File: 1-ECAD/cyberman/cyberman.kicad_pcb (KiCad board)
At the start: 6 copper layers, 0 parts

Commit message: footpritn day
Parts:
- added J1: 5033981892, 0_connector_smd:5033981892, F.Cu at (133.8, 86.6)
- added J2: YXT-BB10-24S-02, 0_connector_smd:YXT-BB10-24S-02, F.Cu at (162.8, 99.5)
- added J3: 532610271, 0_connector_smd:532610271, F.Cu at (128.7, 115.9)
- added L6: BLM15PX331SZ1D, 0_inductor_smd:BLM15PX331SZ1D, F.Cu at (128.3, 111.2)
- added L7: BLM15PX331SZ1D, 0_inductor_smd:BLM15PX331SZ1D, F.Cu at (129.3, 111.2)
- added U1: ESP32-S3R16V, 0_mcu_espressif:ESP32-S3R16V, F.Cu at (160.6, 87.7)
- added U11: LSM6DSOTR, 0_sensor:LSM6DSOTR, F.Cu at (139.1, 99.2)
- added U12: ICS-43434, 0_sensor:ICS-43434, F.Cu at (134.8, 107.3)
- added U13: MAX98357A, 0_CI_smd:MAX98357AETE+T, F.Cu at (129.3, 107.9)
- added U15: W25Q128JWPIQ, 0_CI_smd:W25Q128JWPIQ, F.Cu at (160.2, 77.2)
- added U16: 1054500101, 0_connector_smd:1054500101, F.Cu at (161.6, 68.5)
- added U18: PM254-2-10-W-8.5, 0_connector_smd:PM254-2-10-W-8.5, F.Cu at (151.2, 74.1)
- added U2: BQ25896RTWR, 0_CI_smd:BQ25896RTWR, F.Cu at (147.3, 100.4)
- added U20: LIS2MDLTR, 0_sensor:LIS2MDLTR, F.Cu at (139.7, 107.0)
- added U4: BQ27220YZFR, 0_CI_smd:BQ27220YZFR, F.Cu at (145.6, 109.2)
- added U5: RS3221-3.3YF3, 0_converter_DCDC:RS3221-3.3YF3, F.Cu at (153.2, 106.4)
- added U6: LM3281YFQR, 0_converter_DCDC:LM3281YFQR, F.Cu at (145.4, 105.6)
- added U7: LM3281YFQR, 0_converter_DCDC:LM3281YFQR, F.Cu at (148.7, 105.6)
- added U8: MMDT2907A-7-F, 0_CI_smd:MMDT2907A-7-F, F.Cu at (153.1, 98.9)

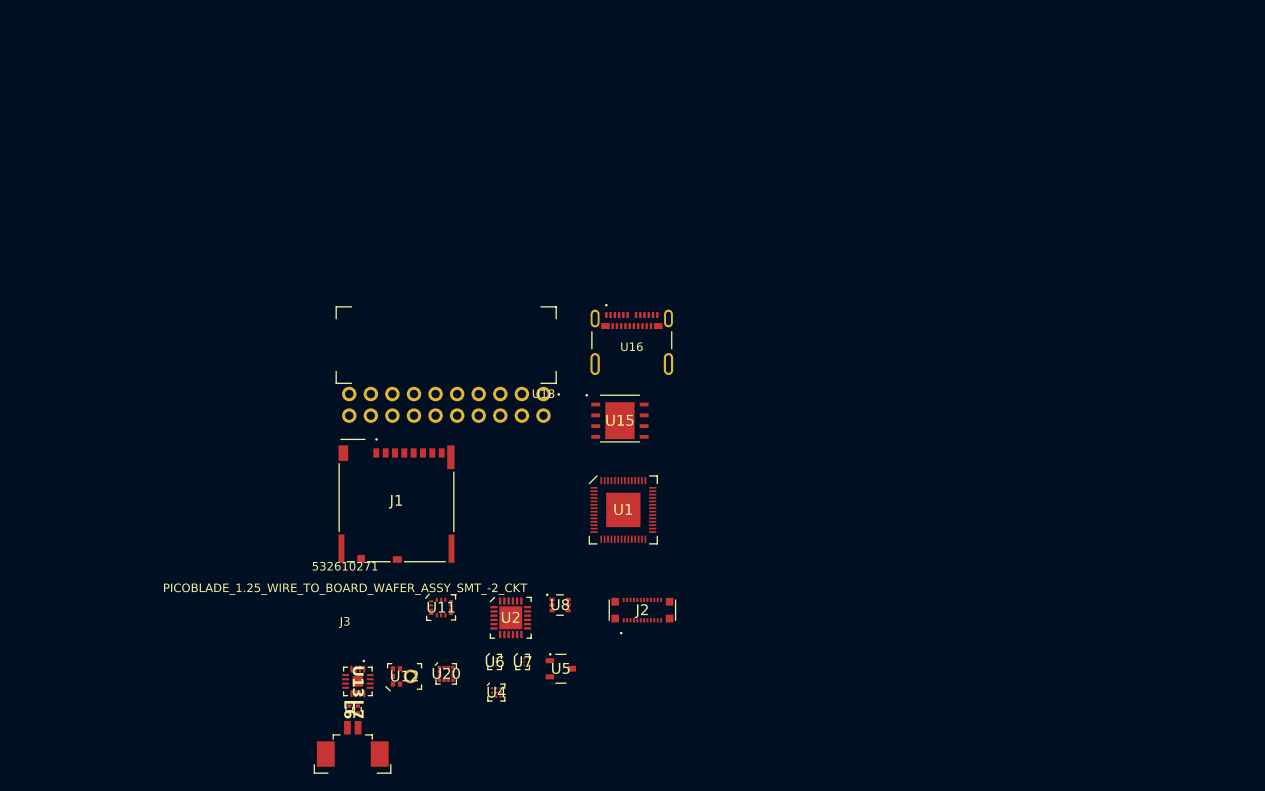
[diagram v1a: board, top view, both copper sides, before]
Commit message: sensor page closed
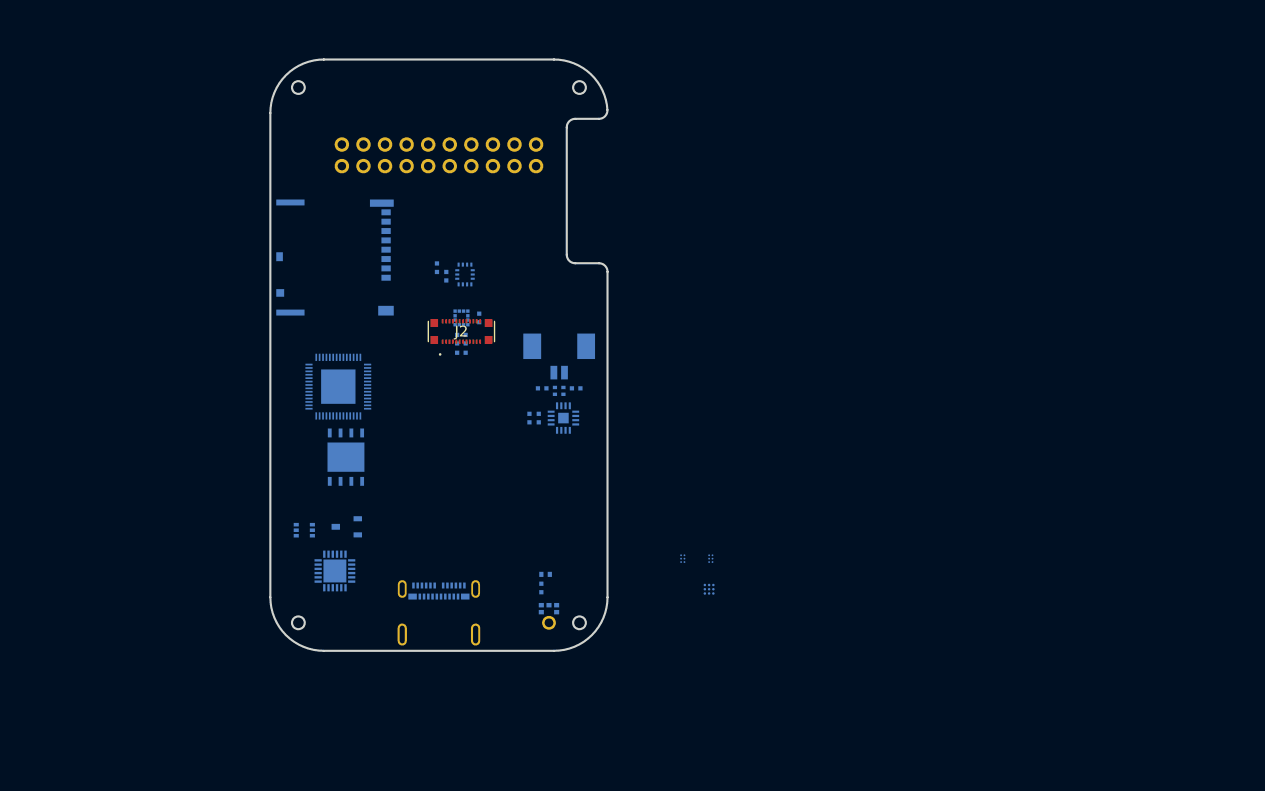
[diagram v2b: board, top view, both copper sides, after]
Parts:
- added C34: CC0402KRX7R8BB104, 0_capacitor_smd:C_0402, B.Cu at (138.6, 59.2)
- added C35: CC0402KRX7R8BB104, 0_capacitor_smd:C_0402, B.Cu at (139.7, 60.2)
- added C36: CC0402KRX7R8BB104, 0_capacitor_smd:C_0402, B.Cu at (141.5, 67.1)
- added C37: CC0402KRX7R8BB104, 0_capacitor_smd:C_0402, B.Cu at (141.5, 68.1)
- added C38: CC0402MRX5R6BB106, 0_capacitor_smd:C_0402, B.Cu at (141.5, 69.2)
- added C39: CC0402KRX7R8BB104, 0_capacitor_smd:C_0402, B.Cu at (150.9, 96.9)
- added C40: CC0402KRX7R8BB104, 0_capacitor_smd:C_0402, B.Cu at (150.6, 76.9)
- added C41: CC0402MRX5R6BB106, 0_capacitor_smd:C_0402, B.Cu at (149.5, 76.9)
- added C49: CC0402KRX5R8BB224, 0_capacitor_smd:C_0402, B.Cu at (143.6, 65.1)
- added C52: CC0402KRX7R8BB221, 0_capacitor_smd:C_0402, B.Cu at (155.0, 73.4)
- added C53: CC0402KRX7R8BB221, 0_capacitor_smd:C_0402, B.Cu at (151.0, 73.4)
- added R27: RC0402FR-07100KL, 0_resistor_smd:R_0402, B.Cu at (151.4, 95.3)
- J1, J3, L6, L7, U1, U11, U12, U13, U15, U16, U18, U2, U20, U4, U5, U6, U7, U8: moved to B.Cu
- moved J3 52.8 mm to (153.0, 69.0)
- moved L6 44.6 mm to (152.5, 73.7), turned to 90 degrees
- moved L7 44.6 mm to (153.5, 73.7), turned to 90 degrees
- moved U20 41.9 mm to (141.5, 65.1), turned to -90 degrees
- moved U13 39.3 mm to (153.5, 76.9), turned to 90 degrees
- moved U11 39.3 mm to (141.9, 60.0), turned to 90 degrees
- moved J2 39.1 mm to (141.5, 66.7)
- moved U16 39.1 mm to (138.8, 100.4), turned to 180 degrees
- moved U18 37.8 mm to (127.4, 44.7), turned to 180 degrees
- moved U1 36.6 mm to (127.0, 73.2), turned to -90 degrees
- moved U15 32.5 mm to (127.9, 81.5), turned to 90 degrees
- moved U8 31.4 mm to (123.0, 90.1), turned to 180 degrees
- moved U5 30.2 mm to (128.0, 89.7), turned to 180 degrees
- moved J1 29.4 mm to (127.0, 58.0), turned to 90 degrees
- moved U6 28.2 mm to (170.8, 93.5), turned to 180 degrees
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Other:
- board outline added: 39.7 x 69.6 mm
- copper layers 6 -> 4

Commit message: add buttons
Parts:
- added SW1: SKRMAAE010, 0_switch:SKRMAAE010, F.Cu at (149.1, 83.8)
- added SW2: SKRMAAE010, 0_switch:SKRMAAE010, F.Cu at (149.1, 94.2)
- added SW3: SKRMAAE010, 0_switch:SKRMAAE010, F.Cu at (130.5, 81.5)
- added SW4: SKRMAAE010, 0_switch:SKRMAAE010, F.Cu at (138.0, 89.0)
- added SW5: SKRMAAE010, 0_switch:SKRMAAE010, F.Cu at (123.0, 89.0)
- added SW6: SKRMAAE010, 0_switch:SKRMAAE010, F.Cu at (130.5, 96.5)
- moved C39 25.8 mm to (125.1, 96.9)
- moved C52 25.8 mm to (129.2, 73.4)
- moved R27 25.8 mm to (125.6, 95.3)
- moved U12 25.8 mm to (126.0, 100.3)
- moved C40 25.8 mm to (124.8, 76.9)
- moved C41 25.8 mm to (123.7, 76.9)
- moved C53 25.8 mm to (125.2, 73.4)
- moved J3 25.8 mm to (127.2, 69.0)
- moved L6 25.8 mm to (126.7, 73.7)
- moved L7 25.8 mm to (127.7, 73.7)
- moved U13 25.8 mm to (127.7, 76.9)
- moved J1 24.8 mm to (151.7, 59.6)
- moved U1 24.5 mm to (151.4, 74.8)
- moved U15 24.5 mm to (152.3, 83.1)
- moved U2 24.5 mm to (151.0, 96.5)
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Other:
- outline, holes or cut-outs redrawn

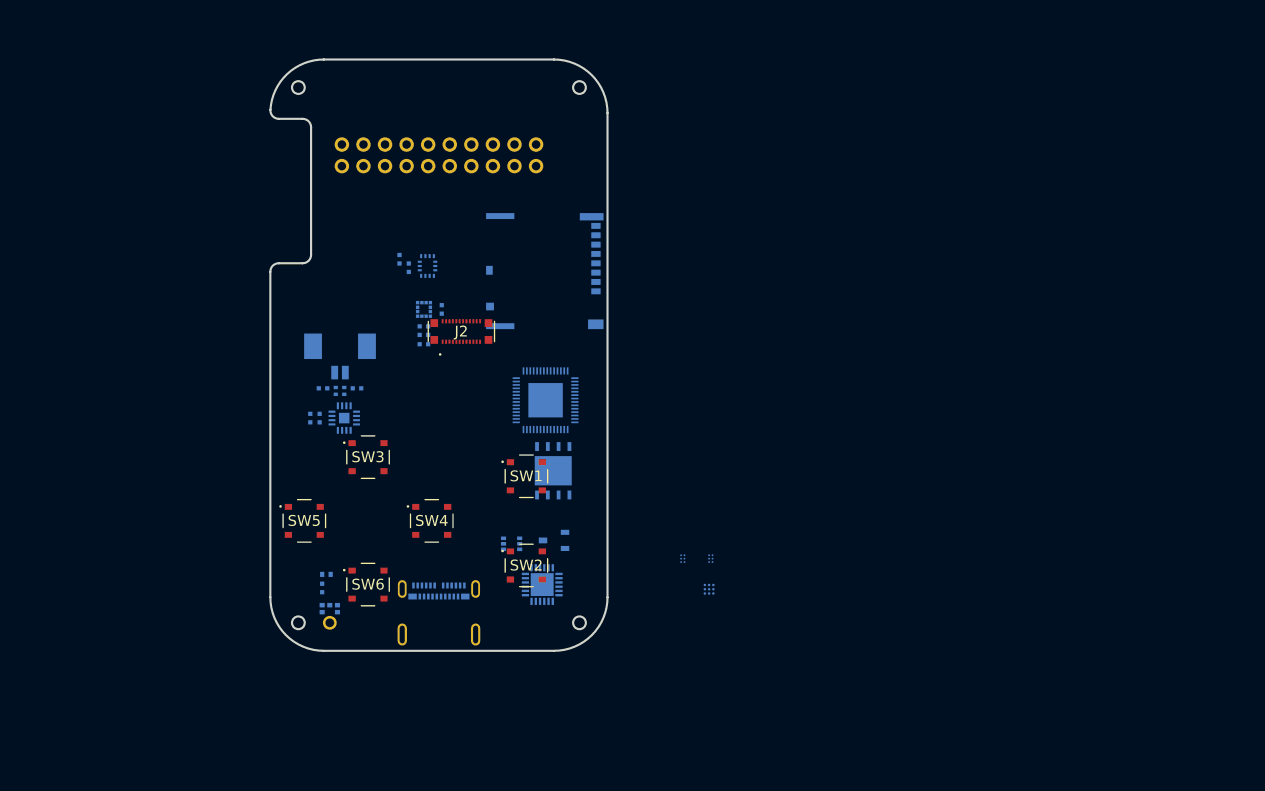
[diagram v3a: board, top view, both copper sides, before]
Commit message: new changes
close display page and peripheral schematic
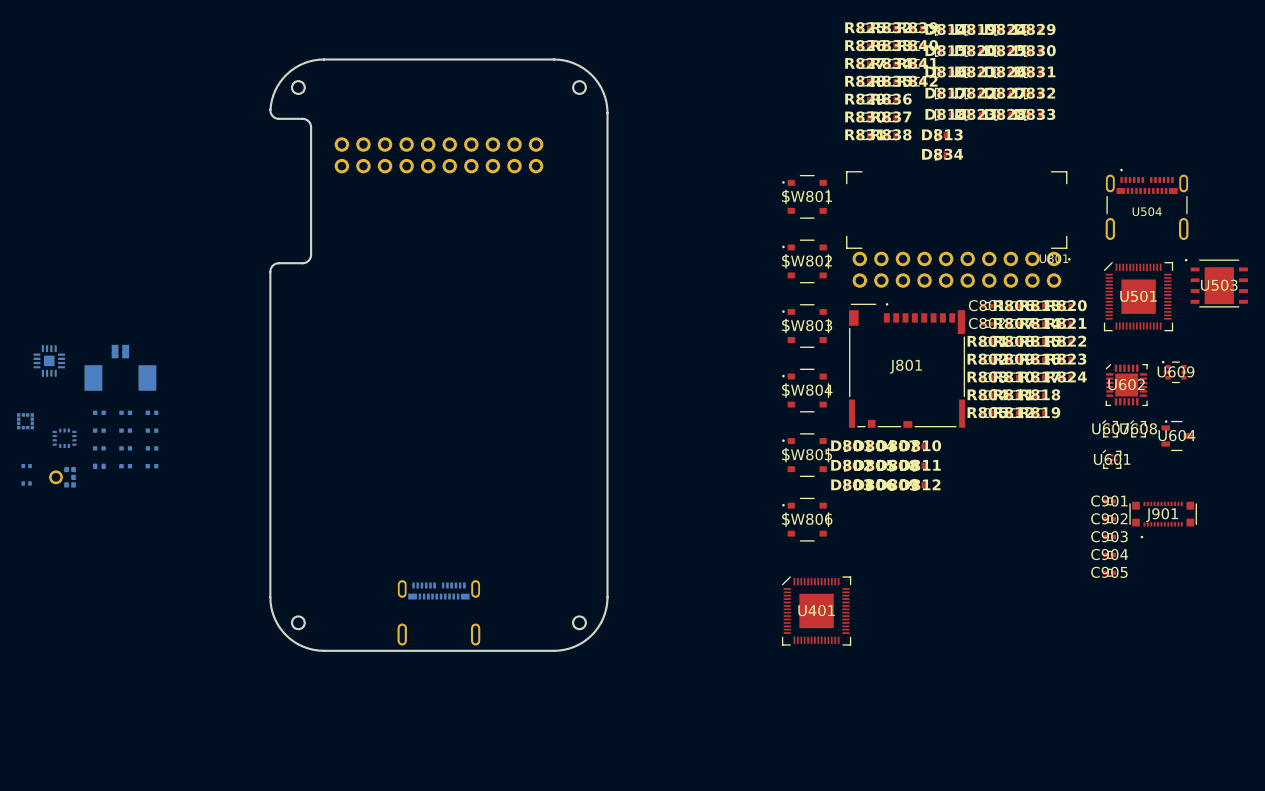
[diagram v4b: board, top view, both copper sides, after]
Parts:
- removed C34, C35, C36, C37, C39, C40: CC0402KRX7R8BB104, 0_capacitor_smd:C_0402
- removed C38, C41: CC0402MRX5R6BB106, 0_capacitor_smd:C_0402
- removed C49: CC0402KRX5R8BB224, 0_capacitor_smd:C_0402
- removed C52, C53: CC0402KRX7R8BB221, 0_capacitor_smd:C_0402
- removed J1: 5033981892, 0_connector_smd:5033981892
- removed J2: YXT-BB10-24S-02, 0_connector_smd:YXT-BB10-24S-02
- removed J3: 532610271, 0_connector_smd:532610271
- removed L6, L7: BLM15PX331SZ1D, 0_inductor_smd:BLM15PX331SZ1D
- removed R27: RC0402FR-07100KL, 0_resistor_smd:R_0402
- removed SW1, SW2, SW3, SW4, SW5, SW6: SKRMAAE010, 0_switch:SKRMAAE010
- removed U1: ESP32-S3R16V, 0_mcu_espressif:ESP32-S3R16V
- removed U11: LSM6DSOTR, 0_sensor:LSM6DSOTR
- removed U12: ICS-43434, 0_sensor:ICS-43434
- removed U13: MAX98357A, 0_CI_smd:MAX98357AETE+T
- removed U15: W25Q128JWPIQ, 0_CI_smd:W25Q128JWPIQ
- removed U2: BQ25896RTWR, 0_CI_smd:BQ25896RTWR
- removed U20: LIS2MDLTR, 0_sensor:LIS2MDLTR
- removed U4: BQ27220YZFR, 0_CI_smd:BQ27220YZFR
- removed U5: RS3221-3.3YF3, 0_converter_DCDC:RS3221-3.3YF3
- removed U6, U7: LM3281YFQR, 0_converter_DCDC:LM3281YFQR
- removed U8: MMDT2907A-7-F, 0_CI_smd:MMDT2907A-7-F
- added C1001: CC0402MRX5R6BB106, 0_capacitor_smd:C_0402, B.Cu at (105.1, 76.3)
- added C1002: CC0402KRX7R8BB104, 0_capacitor_smd:C_0402, B.Cu at (105.1, 78.4)
- added C1003: CC0402KRX7R8BB104, 0_capacitor_smd:C_0402, B.Cu at (105.1, 80.5)
- added C1004: CC0402KRX7R8BB221, 0_capacitor_smd:C_0402, B.Cu at (105.1, 82.6)
- added C1005: CC0402KRX7R8BB221, 0_capacitor_smd:C_0402, B.Cu at (102.0, 76.3)
- added C1006: CC0402MRX5R6BB106, 0_capacitor_smd:C_0402, B.Cu at (102.0, 78.4)
- added C1007: CC0402KRX7R8BB104, 0_capacitor_smd:C_0402, B.Cu at (102.0, 80.5)
- added C1008: CC0402KRX7R8BB104, 0_capacitor_smd:C_0402, B.Cu at (102.0, 82.6)
- added C1009: CC0402KRX7R8BB104, 0_capacitor_smd:C_0402, B.Cu at (98.9, 76.3)
- added C1010: CC0402KRX7R8BB104, 0_capacitor_smd:C_0402, B.Cu at (98.9, 78.4)
- added C1011: CC0402KRX5R8BB224, 0_capacitor_smd:C_0402, B.Cu at (98.9, 80.5)
- added C801: CC0402MRX5R6BB106, 0_capacitor_smd:C_0402, F.Cu at (203.4, 63.7)
- added C802: CC0402MRX5R6BB106, 0_capacitor_smd:C_0402, F.Cu at (203.4, 65.8)
- added C901: CC0402MRX5R6BB106, 0_capacitor_smd:C_0402, F.Cu at (217.8, 86.7)
- added C902: CC0402KRX7R8BB104, 0_capacitor_smd:C_0402, F.Cu at (217.8, 88.8)
- added C903: CC0402KRX7R8BB104, 0_capacitor_smd:C_0402, F.Cu at (217.8, 90.9)
- added C904: CC0402MRX5R6BB106, 0_capacitor_smd:C_0402, F.Cu at (217.8, 93.0)
- added C905: CC0402KRX7R8BB104, 0_capacitor_smd:C_0402, F.Cu at (217.8, 95.1)
- added D801: LESD8D3.3CAT5G, 0_diode_smd:LESD8D3.3CAT5G, F.Cu at (187.4, 80.2)
- added D802: LESD8D3.3CAT5G, 0_diode_smd:LESD8D3.3CAT5G, F.Cu at (187.4, 82.5)
- added D803: LESD8D3.3CAT5G, 0_diode_smd:LESD8D3.3CAT5G, F.Cu at (187.4, 84.8)
- added D804: LESD8D3.3CAT5G, 0_diode_smd:LESD8D3.3CAT5G, F.Cu at (190.1, 80.2)
- added D805: LESD8D3.3CAT5G, 0_diode_smd:LESD8D3.3CAT5G, F.Cu at (190.1, 82.5)
- added D806: LESD8D3.3CAT5G, 0_diode_smd:LESD8D3.3CAT5G, F.Cu at (190.1, 84.8)
- added D807: LESD8D3.3CAT5G, 0_diode_smd:LESD8D3.3CAT5G, F.Cu at (192.8, 80.2)
- added D808: LESD8D3.3CAT5G, 0_diode_smd:LESD8D3.3CAT5G, F.Cu at (192.8, 82.5)
- added D809: LESD8D3.3CAT5G, 0_diode_smd:LESD8D3.3CAT5G, F.Cu at (192.8, 84.8)
- added D810: LESD8D3.3CAT5G, 0_diode_smd:LESD8D3.3CAT5G, F.Cu at (195.5, 80.2)
- added D811: LESD8D3.3CAT5G, 0_diode_smd:LESD8D3.3CAT5G, F.Cu at (195.5, 82.5)
- added D812: LESD8D3.3CAT5G, 0_diode_smd:LESD8D3.3CAT5G, F.Cu at (195.5, 84.8)
- added D813: LESD8D3.3CAT5G, 0_diode_smd:LESD8D3.3CAT5G, F.Cu at (198.1, 43.6)
- added D814: LESD5D5.0CT1G, 0_diode_smd:LESD5D5.0CT1G, F.Cu at (198.5, 31.2)
- added D815: LESD5D5.0CT1G, 0_diode_smd:LESD5D5.0CT1G, F.Cu at (198.5, 33.7)
- added D816: LESD5D5.0CT1G, 0_diode_smd:LESD5D5.0CT1G, F.Cu at (198.5, 36.2)
- added D817: LESD5D5.0CT1G, 0_diode_smd:LESD5D5.0CT1G, F.Cu at (198.5, 38.7)
- added D818: LESD5D5.0CT1G, 0_diode_smd:LESD5D5.0CT1G, F.Cu at (198.5, 41.2)
- added D819: LESD5D5.0CT1G, 0_diode_smd:LESD5D5.0CT1G, F.Cu at (202.0, 31.2)
- added D820: LESD5D5.0CT1G, 0_diode_smd:LESD5D5.0CT1G, F.Cu at (202.0, 33.7)
- added D821: LESD5D5.0CT1G, 0_diode_smd:LESD5D5.0CT1G, F.Cu at (202.0, 36.2)
- added D822: LESD5D5.0CT1G, 0_diode_smd:LESD5D5.0CT1G, F.Cu at (202.0, 38.7)
- added D823: LESD5D5.0CT1G, 0_diode_smd:LESD5D5.0CT1G, F.Cu at (202.0, 41.2)
- added D824: LESD5D5.0CT1G, 0_diode_smd:LESD5D5.0CT1G, F.Cu at (205.5, 31.2)
- added D825: LESD5D5.0CT1G, 0_diode_smd:LESD5D5.0CT1G, F.Cu at (205.5, 33.7)
- added D826: LESD5D5.0CT1G, 0_diode_smd:LESD5D5.0CT1G, F.Cu at (205.5, 36.2)
- added D827: LESD5D5.0CT1G, 0_diode_smd:LESD5D5.0CT1G, F.Cu at (205.5, 38.7)
- added D828: LESD5D5.0CT1G, 0_diode_smd:LESD5D5.0CT1G, F.Cu at (205.5, 41.2)
- added D829: LESD5D5.0CT1G, 0_diode_smd:LESD5D5.0CT1G, F.Cu at (209.0, 31.2)
- added D830: LESD5D5.0CT1G, 0_diode_smd:LESD5D5.0CT1G, F.Cu at (209.0, 33.7)
- added D831: LESD5D5.0CT1G, 0_diode_smd:LESD5D5.0CT1G, F.Cu at (209.0, 36.2)
- added D832: LESD5D5.0CT1G, 0_diode_smd:LESD5D5.0CT1G, F.Cu at (209.0, 38.7)
- added D833: LESD5D5.0CT1G, 0_diode_smd:LESD5D5.0CT1G, F.Cu at (209.0, 41.2)
- added D834: LESD8D3.3CAT5G, 0_diode_smd:LESD8D3.3CAT5G, F.Cu at (198.1, 45.9)
- added J1001: 532610271, 0_connector_smd:532610271, B.Cu at (101.3, 71.6)
- added J801: 5033981892, 0_connector_smd:5033981892, F.Cu at (193.9, 70.7)
- added J901: YXT-BB10-24S-02, 0_connector_smd:YXT-BB10-24S-02, F.Cu at (224.1, 88.2)
- added L1001: BLM15PX331SZ1D, 0_inductor_smd:BLM15PX331SZ1D, B.Cu at (90.3, 82.5)
- added L1002: BLM15PX331SZ1D, 0_inductor_smd:BLM15PX331SZ1D, B.Cu at (90.3, 84.6)
- added R1001: RC0402FR-07100KL, 0_resistor_smd:R_0402, B.Cu at (98.9, 82.6)
- added R801: RC0402FR-0747KL, 0_resistor_smd:R_0402, F.Cu at (203.4, 67.9)
- added R802: RC0402FR-0747KL, 0_resistor_smd:R_0402, F.Cu at (203.4, 70.0)
- added R803: RC0402FR-0747KL, 0_resistor_smd:R_0402, F.Cu at (203.4, 72.1)
- added R804: RC0402FR-0747KL, 0_resistor_smd:R_0402, F.Cu at (203.4, 74.2)
- added R805: RC0402FR-0747KL, 0_resistor_smd:R_0402, F.Cu at (203.4, 76.3)
- added R806: RC0402FR-0747KL, 0_resistor_smd:R_0402, F.Cu at (206.5, 63.7)
- added R807: RC0402FR-0747KL, 0_resistor_smd:R_0402, F.Cu at (206.5, 65.8)
- added R808: RC0402FR-0710KL, 0_resistor_smd:R_0402, F.Cu at (206.5, 67.9)
- added R809: RC0402FR-0710KL, 0_resistor_smd:R_0402, F.Cu at (206.5, 70.0)
- added R810: RC0402FR-0710KL, 0_resistor_smd:R_0402, F.Cu at (206.5, 72.1)
- added R811: RC0402FR-0710KL, 0_resistor_smd:R_0402, F.Cu at (206.5, 74.2)
- added R812: RC0402FR-0710KL, 0_resistor_smd:R_0402, F.Cu at (206.5, 76.3)
- added R813: RC0402FR-0710KL, 0_resistor_smd:R_0402, F.Cu at (209.6, 63.7)
- added R814: RC0402FR-07330RL, 0_resistor_smd:R_0402, F.Cu at (209.6, 65.8)
- added R815: RC0402FR-07150RL, 0_resistor_smd:R_0402, F.Cu at (209.6, 67.9)
- added R816: RC0402FR-0751RL, 0_resistor_smd:R_0402, F.Cu at (209.6, 70.0)
- added R817: RC0402FR-0751RL, 0_resistor_smd:R_0402, F.Cu at (209.6, 72.1)
- added R818: RC0402FR-07330RL, 0_resistor_smd:R_0402, F.Cu at (209.6, 74.2)
- added R819: RC0402FR-0751RL, 0_resistor_smd:R_0402, F.Cu at (209.6, 76.3)
- added R820: RC0402FR-07150RL, 0_resistor_smd:R_0402, F.Cu at (212.7, 63.7)
- added R821: RC0402FR-07330RL, 0_resistor_smd:R_0402, F.Cu at (212.7, 65.8)
- added R822: RC0402FR-07330RL, 0_resistor_smd:R_0402, F.Cu at (212.7, 67.9)
- added R823: RC0402FR-07330RL, 0_resistor_smd:R_0402, F.Cu at (212.7, 70.0)
- added R824: RC0402FR-07330RL, 0_resistor_smd:R_0402, F.Cu at (212.7, 72.1)
- added R825: RC0402FR-0751RL, 0_resistor_smd:R_0402, F.Cu at (189.0, 31.0)
- added R826: RC0402FR-0751RL, 0_resistor_smd:R_0402, F.Cu at (189.0, 33.1)
- added R827: RC0402FR-0751RL, 0_resistor_smd:R_0402, F.Cu at (189.0, 35.2)
- added R828: RC0402FR-0751RL, 0_resistor_smd:R_0402, F.Cu at (189.0, 37.3)
- added R829: RC0402FR-0751RL, 0_resistor_smd:R_0402, F.Cu at (189.0, 39.4)
- added R830: RC0402FR-0751RL, 0_resistor_smd:R_0402, F.Cu at (189.0, 41.5)
- added R831: RC0402FR-0751RL, 0_resistor_smd:R_0402, F.Cu at (189.0, 43.6)
- added R832: RC0402FR-0751RL, 0_resistor_smd:R_0402, F.Cu at (192.1, 31.0)
- added R833: RC0402FR-0751RL, 0_resistor_smd:R_0402, F.Cu at (192.1, 33.1)
- added R834: RC0402FR-0751RL, 0_resistor_smd:R_0402, F.Cu at (192.1, 35.2)
- added R835: RC0402FR-0751RL, 0_resistor_smd:R_0402, F.Cu at (192.1, 37.3)
- added R836: RC0402FR-0751RL, 0_resistor_smd:R_0402, F.Cu at (192.1, 39.4)
- added R837: RC0402FR-0751RL, 0_resistor_smd:R_0402, F.Cu at (192.1, 41.5)
- added R838: RC0402FR-0751RL, 0_resistor_smd:R_0402, F.Cu at (192.1, 43.6)
- added R839: RC0402FR-0751RL, 0_resistor_smd:R_0402, F.Cu at (195.2, 31.0)
- added R840: RC0402FR-0751RL, 0_resistor_smd:R_0402, F.Cu at (195.2, 33.1)
- added R841: RC0402FR-0751RL, 0_resistor_smd:R_0402, F.Cu at (195.2, 35.2)
- added R842: RC0402FR-0751RL, 0_resistor_smd:R_0402, F.Cu at (195.2, 37.3)
- added SW801: SKRMAAE010, 0_switch:SKRMAAE010, F.Cu at (182.2, 50.9)
- added SW802: SKRMAAE010, 0_switch:SKRMAAE010, F.Cu at (182.2, 58.5)
- added SW803: SKRMAAE010, 0_switch:SKRMAAE010, F.Cu at (182.2, 66.1)
- added SW804: SKRMAAE010, 0_switch:SKRMAAE010, F.Cu at (182.2, 73.7)
- added SW805: SKRMAAE010, 0_switch:SKRMAAE010, F.Cu at (182.2, 81.3)
- added SW806: SKRMAAE010, 0_switch:SKRMAAE010, F.Cu at (182.2, 88.9)
- added U1001: MAX98357A, 0_CI_smd:MAX98357AETE+T, B.Cu at (93.0, 70.2)
- added U1002: ICS-43434, 0_sensor:ICS-43434, B.Cu at (94.5, 83.9)
- added U1003: LIS2MDLTR, 0_sensor:LIS2MDLTR, B.Cu at (90.2, 77.3)
- added U1004: LSM6DSOTR, 0_sensor:LSM6DSOTR, B.Cu at (94.8, 79.3)
- added U401: ESP32-S3R16V, 0_mcu_espressif:ESP32-S3R16V, F.Cu at (183.3, 99.6)
- added U501: ESP32-S3R16V, 0_mcu_espressif:ESP32-S3R16V, F.Cu at (221.2, 62.6)
- added U503: W25Q128JWPIQ, 0_CI_smd:W25Q128JWPIQ, F.Cu at (230.7, 61.3)
- added U504: 1054500101, 0_connector_smd:1054500101, F.Cu at (222.2, 52.6)
- added U601: BQ27220YZFR, 0_CI_smd:BQ27220YZFR, F.Cu at (218.1, 81.8)
- added U602: BQ25896RTWR, 0_CI_smd:BQ25896RTWR, F.Cu at (219.8, 73.0)
- added U604: RS3221-3.3YF3, 0_converter_DCDC:RS3221-3.3YF3, F.Cu at (225.7, 79.0)
- added U607: LM3281YFQR, 0_converter_DCDC:LM3281YFQR, F.Cu at (217.9, 78.2)
- added U608: LM3281YFQR, 0_converter_DCDC:LM3281YFQR, F.Cu at (221.2, 78.2)
- added U609: MMDT2907A-7-F, 0_CI_smd:MMDT2907A-7-F, F.Cu at (225.6, 71.5)
- added U801: PM254-2-10-W-8.5, 0_connector_smd:PM254-2-10-W-8.5, F.Cu at (211.2, 58.2)
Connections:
- U16 pad A10: unconnected-(U16-RX2--PadA10) -> (no net)
- U16 pad A11: unconnected-(U16-RX2+-PadA11) -> (no net)
- U16 pad A2: unconnected-(U16-TX1+-PadA2) -> (no net)
- U16 pad A3: unconnected-(U16-TX1--PadA3) -> (no net)
- U16 pad A5: Net-(U16-CC1) -> unconnected-(R32-Pad1)
- U16 pad A6: Net-(C46-Pad1) -> (no net)
- U16 pad A8: unconnected-(U16-SBU1-PadA8) -> (no net)
- U16 pad B10: unconnected-(U16-RX1--PadB10) -> (no net)
- U16 pad B11: unconnected-(U16-RX1+-PadB11) -> (no net)
- U16 pad B2: unconnected-(U16-TX2+-PadB2) -> (no net)
- U16 pad B3: unconnected-(U16-TX2--PadB3) -> (no net)
- U16 pad B5: Net-(U16-CC2) -> (no net)
- U16 pad B6: Net-(C46-Pad1) -> (no net)
- U16 pad B8: unconnected-(U16-SBU2-PadB8) -> (no net)
